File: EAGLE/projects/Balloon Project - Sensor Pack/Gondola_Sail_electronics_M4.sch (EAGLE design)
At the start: 8 parts

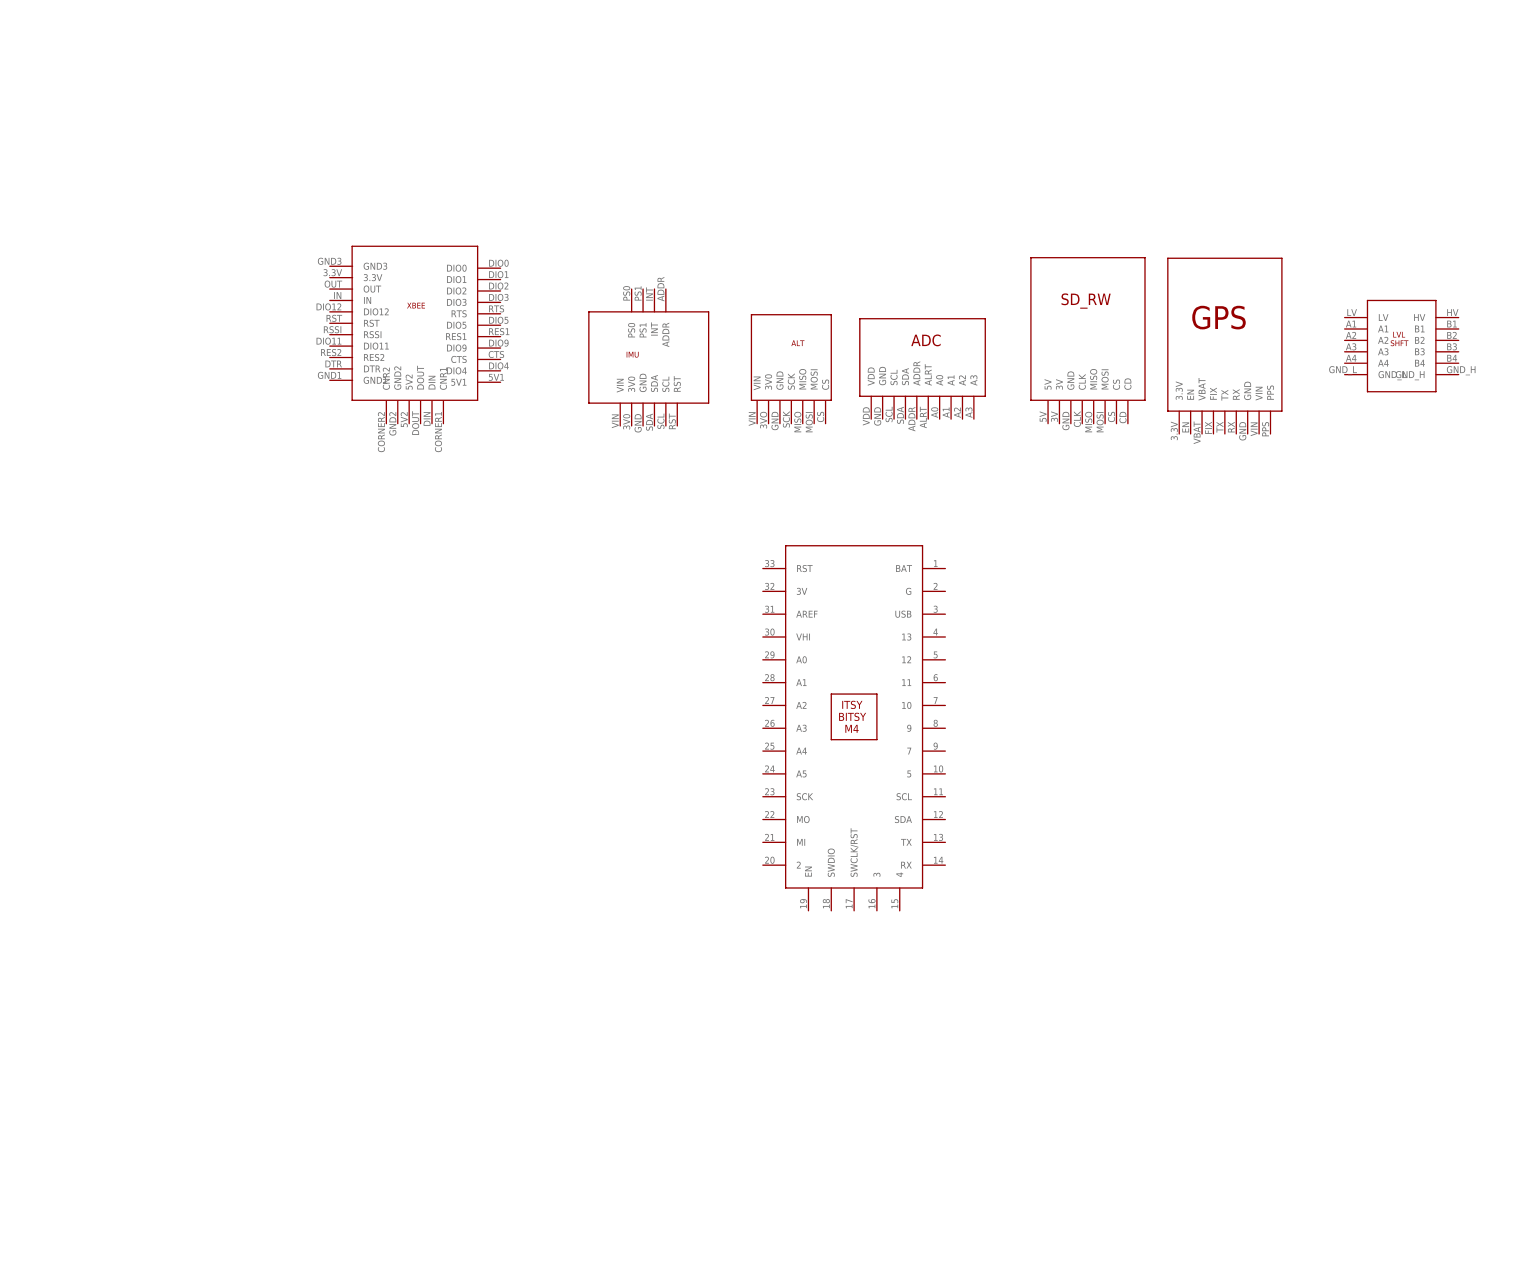
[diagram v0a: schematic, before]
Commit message: building pcb schematic
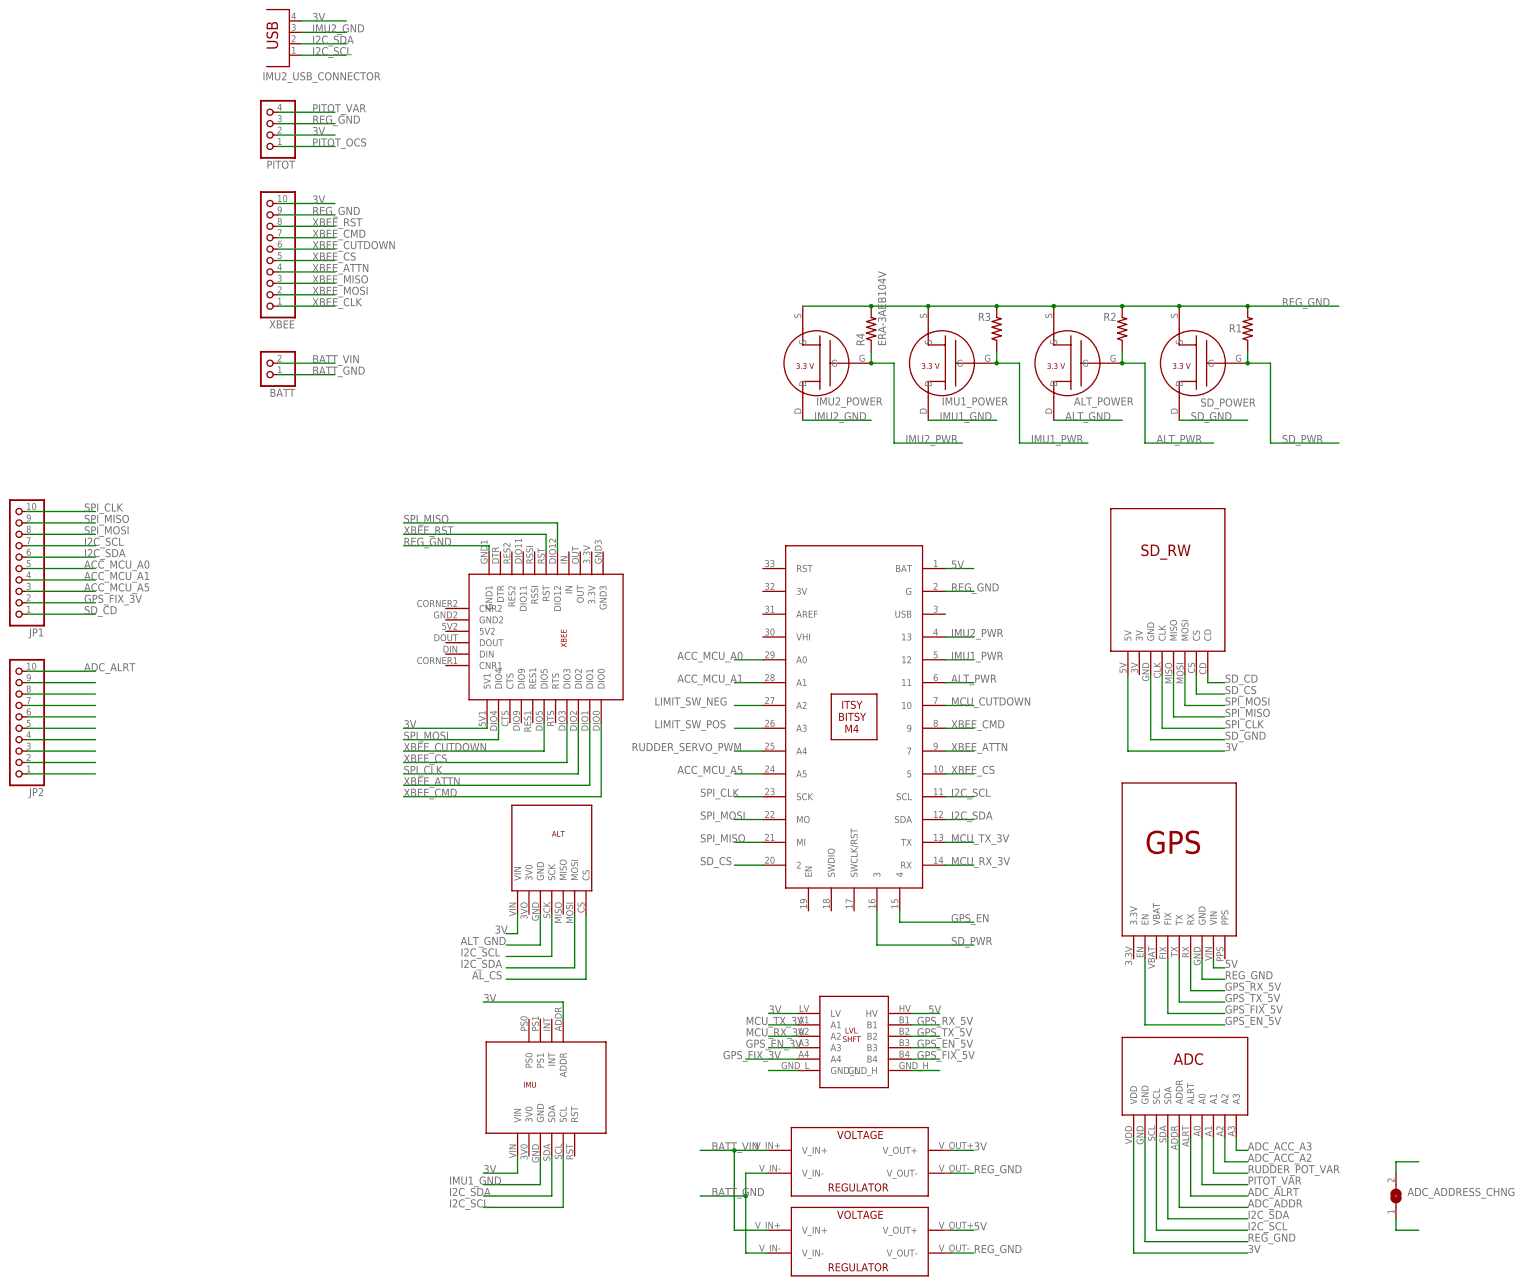
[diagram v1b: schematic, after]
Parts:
- removed U$5: BNO055, Adafruit_Arduino:BNO055
- added 3V_REG, 5V_REG: 3V/5V_REGULATOR, Adafruit_Arduino:3V/5V_REGULATOR
- added ADC_ADDRESS_CHNG: (no value), jumper:SJ
- added ALT_POWER, IMU1_POWER, IMU2_POWER, SD_POWER: 3.3V_NCH_FET, Adafruit_Arduino:3.3V_NCH_FET
- added BATT: (no value), pinhead:PINHD-1X2/90
- added IMU1: BNO055, Adafruit_Arduino:BNO055
- added IMU2_USB_CONNECTOR: (no value), con-berg:PN87520
- added JP1, JP2, XBEE: (no value), pinhead:PINHD-1X10/90
- added PITOT: (no value), pinhead:PINHD-1X4/90
- added R1, R2, R3, R4: ERA-3AEB104V, ERA-3AEB104V:ERA-3AEB104V
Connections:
- new net 3V: 3V_REG.V_OUT+, IMU1.ADDR, IMU1.VIN, IMU2_USB_CONNECTOR.4, PITOT.2, U$2.5V, U$3.VDD, U$4.VIN, U$6.LV, U$7.5V1, XBEE.10
- new net 5V: 5V_REG.V_OUT+, U$1.VIN, U$6.HV, U$8.BAT
- new net ACC_MCU_A0: JP1.5, U$8.A0
- new net ACC_MCU_A1: JP1.4, U$8.A1
- new net ACC_MCU_A5: JP1.3, U$8.A5
- new net ADC_ACC_A2: U$3.A2
- new net ADC_ACC_A3: U$3.A3
- new net ADC_ADDR: U$3.ADDR
- new net ADC_ALRT: JP2.10, U$3.ALRT
- new net ALT_GND: ALT_POWER.D, U$4.GND
- new net ALT_PWR: ALT_POWER.G, R2.1, U$8.11
- new net AL_CS: U$4.CS
- new net BATT_GND: 3V_REG.V_IN-, 5V_REG.V_IN-, BATT.1
- new net BATT_VIN: 3V_REG.V_IN+, 5V_REG.V_IN+, BATT.2
- new net GPS_EN: U$8.4
- new net GPS_EN_3V: U$6.A3
- new net GPS_EN_5V: U$1.EN, U$6.B3
- new net GPS_FIX_3V: JP1.2, U$6.A4
- new net GPS_FIX_5V: U$1.FIX, U$6.B4
- new net GPS_RX_5V: U$1.RX, U$6.B1
- new net GPS_TX_5V: U$1.TX, U$6.B2
- new net I2C_SCL: IMU1.SCL, IMU2_USB_CONNECTOR.1, JP1.7, U$3.SCL, U$4.SCK, U$8.SCL
- new net I2C_SDA: IMU1.SDA, IMU2_USB_CONNECTOR.2, JP1.6, U$3.SDA, U$4.MOSI, U$8.SDA
- new net IMU1_GND: IMU1.GND, IMU1_POWER.D
- new net IMU1_PWR: IMU1_POWER.G, R3.1, U$8.12
- new net IMU2_GND: IMU2_POWER.D, IMU2_USB_CONNECTOR.3
- new net IMU2_PWR: IMU2_POWER.G, R4.1, U$8.13
- new net LIMIT_SW_NEG: U$8.A2
- new net LIMIT_SW_POS: U$8.A3
- new net MCU_CUTDOWN: U$8.10
- new net MCU_RX_3V: U$6.A2, U$8.RX
- new net MCU_TX_3V: U$6.A1, U$8.TX
- new net N$1: U$6.GND_L
- new net N$10: JP2.3
- new net N$11: JP2.2
- new net N$12: JP2.1
- new net N$13: ADC_ADDRESS_CHNG.1
- new net N$2: U$6.GND_H
- new net N$3: ADC_ADDRESS_CHNG.2
- new net N$4: JP2.9
- new net N$5: JP2.8
- new net N$6: JP2.7
- new net N$7: JP2.6
- new net N$8: JP2.5
- new net N$9: JP2.4
- new net PITOT_OCS: PITOT.1
- new net PITOT_VAR: PITOT.4, U$3.A0
- new net REG_GND: 3V_REG.V_OUT-, 5V_REG.V_OUT-, ALT_POWER.S, IMU1_POWER.S, IMU2_POWER.S, PITOT.3, R1.2, R2.2, R3.2, R4.2, SD_POWER.S, U$1.GND, U$3.GND, U$7.GND1, U$8.G, XBEE.9
- new net RUDDER_POT_VAR: U$3.A1
- new net RUDDER_SERVO_PWM: U$8.A4
- new net SD_CD: JP1.1, U$2.CD
- new net SD_CS: U$2.CS, U$8.2
- new net SD_GND: SD_POWER.D, U$2.GND
- new net SD_PWR: R1.1, SD_POWER.G, U$8.3
- new net SPI_CLK: JP1.10, U$2.CLK, U$7.DIO2, U$8.SCK
- new net SPI_MISO: JP1.9, U$2.MISO, U$7.DIO12, U$8.MI
- new net SPI_MOSI: JP1.8, U$2.MOSI, U$7.DIO4, U$8.MO
- new net XBEE_ATTN: U$7.DIO1, U$8.7, XBEE.4
- new net XBEE_CLK: XBEE.1
- new net XBEE_CMD: U$7.DIO0, U$8.9, XBEE.7
- new net XBEE_CS: U$7.DIO3, U$8.5, XBEE.5
- new net XBEE_CUTDOWN: U$7.DIO5, XBEE.6
- new net XBEE_MISO: XBEE.3
- new net XBEE_MOSI: XBEE.2
- new net XBEE_RST: U$7.RST, XBEE.8
